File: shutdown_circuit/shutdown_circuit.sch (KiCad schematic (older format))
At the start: 16 parts

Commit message: Not sure
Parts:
- C? (x2): value C -> 1u
- C? (x2): value C -> 10u
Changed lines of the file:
@@
 LIBS:relays
 LIBS:shutdown_circuit-cache
-EELAYER 26 0
+EELAYER 25 0
 EELAYER END
 $Descr A4 11693 8268
@@
 P 1800 1100
 F 0 "C?" H 1915 1146 50  0000 L CNN
-F 1 "C" H 1915 1055 50  0000 L CNN
+F 1 "1u" H 1915 1055 50  0000 L CNN
 F 2 "" H 1838 950 50  0000 C CNN
 F 3 "" H 1800 1100 50  0000 C CNN
@@
 P 2200 1100
 F 0 "C?" H 2315 1146 50  0000 L CNN
-F 1 "C" H 2315 1055 50  0000 L CNN
+F 1 "10u" H 2315 1055 50  0000 L CNN
 F 2 "" H 2238 950 50  0000 C CNN
 F 3 "" H 2200 1100 50  0000 C CNN
@@
 P 3500 1100
 F 0 "C?" H 3615 1146 50  0000 L CNN
-F 1 "C" H 3615 1055 50  0000 L CNN
+F 1 "1u" H 3615 1055 50  0000 L CNN
 F 2 "" H 3538 950 50  0000 C CNN
 F 3 "" H 3500 1100 50  0000 C CNN
@@
 P 3950 1100
 F 0 "C?" H 4065 1146 50  0000 L CNN
-F 1 "C" H 4065 1055 50  0000 L CNN
+F 1 "10u" H 4065 1055 50  0000 L CNN
 F 2 "" H 3988 950 50  0000 C CNN
 F 3 "" H 3950 1100 50  0000 C CNN

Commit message: Shutdown circuit changes, IMD begun
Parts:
- removed P?: +12V GLV, symbol CONN_01X01
- removed P?: Ground GLV, symbol CONN_01X01
- removed P?: CONN_01X04, symbol CONN_01X04
- added P?: MX150_8, symbol MX150_8
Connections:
- wire segments 27 -> 25
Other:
- moved on the sheet: U?B
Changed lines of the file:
@@
 LIBS:contrib
 LIBS:valves
+LIBS:relays
 LIBS:UNCAMotorsports
-LIBS:relays
 LIBS:shutdown_circuit-cache
 EELAYER 25 0
@@
 	3950 950  3950 800
 Connection ~ 3950 950
-$Comp
-L +12V #PWR?
-U 1 1 58B0A6A8
-P 1800 800
-F 0 "#PWR?" H 1800 650 50  0001 C CNN
-F 1 "+12V" H 1815 973 50  0000 C CNN
-F 2 "" H 1800 800 50  0000 C CNN
-F 3 "" H 1800 800 50  0000 C CNN
-	1    1800 800
-	1    0    0    -1
-$EndComp
-Wire Wire Line
-	1800 800  1800 950
-$Comp
-L CONN_01X01 P?
-U 1 1 58B0A6D7
-P 700 950
-F 0 "P?" H 619 725 50  0000 C CNN
-F 1 "+12V GLV" H 619 816 50  0000 C CNN
-F 2 "" H 700 950 50  0000 C CNN
-F 3 "" H 700 950 50  0000 C CNN
-	1    700  950
-	-1   0    0    1
-$EndComp
 Wire Wire Line
 	900  950  1200 950
@@
 Wire Wire Line
 	1800 1350 1800 1250
-$Comp
-L CONN_01X01 P?
-U 1 1 58B0A8F1
-P 700 1450
-F 0 "P?" H 619 1225 50  0000 C CNN
-F 1 "Ground GLV" H 619 1316 50  0000 C CNN
-F 2 "" H 700 1450 50  0000 C CNN
-F 3 "" H 700 1450 50  0000 C CNN
-	1    700  1450
-	-1   0    0    1
-$EndComp
-$Comp
-L GND #PWR?
-U 1 1 58B0A96E
-P 1050 1450
-F 0 "#PWR?" H 1050 1200 50  0001 C CNN
-F 1 "GND" H 1055 1277 50  0000 C CNN
-F 2 "" H 1050 1450 50  0000 C CNN
-F 3 "" H 1050 1450 50  0000 C CNN
-	1    1050 1450
-	1    0    0    -1
-$EndComp
-Wire Wire Line
-	1050 1450 900  1450
 $Comp
 L R R?
@@
 L 74HC20D U?
 U 2 1 58B0B725
-P 3800 4600
-F 0 "U?" H 4341 4653 60  0000 L CNN
-F 1 "74HC20D" H 4341 4547 60  0000 L CNN
-F 2 "" H 3800 4600 60  0001 C CNN
-F 3 "" H 3800 4600 60  0001 C CNN
-	2    3800 4600
+P 6300 3100
+F 0 "U?" H 6841 3153 60  0000 L CNN
+F 1 "74HC20D" H 6841 3047 60  0000 L CNN
+F 2 "" H 6300 3100 60  0001 C CNN
+F 3 "" H 6300 3100 60  0001 C CNN
+	2    6300 3100
 	1    0    0    -1
 $EndComp
@@
 L +5V #PWR?
 U 1 1 58B0B835
-P 3900 4150
-F 0 "#PWR?" H 3900 4000 50  0001 C CNN
-F 1 "+5V" H 3915 4323 50  0000 C CNN
-F 2 "" H 3900 4150 50  0000 C CNN
-F 3 "" H 3900 4150 50  0000 C CNN
-	1    3900 4150
-	1    0    0    -1
-$EndComp
-Wire Wire Line
-	3900 4150 3900 4200
+P 6400 2650
+F 0 "#PWR?" H 6400 2500 50  0001 C CNN
+F 1 "+5V" H 6415 2823 50  0000 C CNN
+F 2 "" H 6400 2650 50  0000 C CNN
+F 3 "" H 6400 2650 50  0000 C CNN
+	1    6400 2650
+	1    0    0    -1
+$EndComp
+Wire Wire Line
+	6400 2650 6400 2700
 $Comp
 L GND #PWR?
 U 1 1 58B0B886
-P 3900 5050
-F 0 "#PWR?" H 3900 4800 50  0001 C CNN
-F 1 "GND" H 3905 4877 50  0000 C CNN
-F 2 "" H 3900 5050 50  0000 C CNN
-F 3 "" H 3900 5050 50  0000 C CNN
-	1    3900 5050
-	1    0    0    -1
-$EndComp
-Wire Wire Line
-	3900 5050 3900 5000
-NoConn ~ 4300 4600
-Wire Wire Line
-	3450 4200 3450 4750
-Connection ~ 3450 4550
-Connection ~ 3450 4650
-Wire Wire Line
-	3900 4200 3450 4200
-Connection ~ 3450 4450
+P 6400 3550
+F 0 "#PWR?" H 6400 3300 50  0001 C CNN
+F 1 "GND" H 6405 3377 50  0000 C CNN
+F 2 "" H 6400 3550 50  0000 C CNN
+F 3 "" H 6400 3550 50  0000 C CNN
+	1    6400 3550
+	1    0    0    -1
+$EndComp
+Wire Wire Line
+	6400 3550 6400 3500
+NoConn ~ 6800 3100
+Wire Wire Line
+	5950 2700 5950 3250
+Connection ~ 5950 3050
+Connection ~ 5950 3150
+Wire Wire Line
+	6400 2700 5950 2700
+Connection ~ 5950 2950
 $Comp
 L GND #PWR?
@@
 Connection ~ 2500 3050
 Connection ~ 2200 2950
-$Comp
-L CONN_01X04 P?
-U 1 1 58B0C0EE
-P 1750 3100
-F 0 "P?" H 1669 2725 50  0000 C CNN
-F 1 "CONN_01X04" H 1669 2816 50  0000 C CNN
-F 2 "" H 1750 3100 50  0000 C CNN
-F 3 "" H 1750 3100 50  0000 C CNN
-	1    1750 3100
-	-1   0    0    1
-$EndComp
 Wire Wire Line
 	2200 2950 2200 3250
@@
 Wire Wire Line
 	4950 2700 4950 2900
+$Comp
+L +12V #PWR?
+U 1 1 58C9C2DE
+P 900 950
+F 0 "#PWR?" H 900 800 50  0001 C CNN
+F 1 "+12V" H 900 1090 50  0000 C CNN
+F 2 "" H 900 950 50  0001 C CNN
+F 3 "" H 900 950 50  0001 C CNN
+	1    900  950
+	1    0    0    -1
+$EndComp
+$Comp
+L MX150_8 P?
+U 1 1 58C9C54A
+P 6050 1300
+F 0 "P?" H 6050 1550 50  0000 C CNN
+F 1 "MX150_8" H 6050 1050 50  0000 C CNN
+F 2 "" H 6050 100 50  0000 C CNN
+F 3 "" H 6050 100 50  0000 C CNN
+	1    6050 1300
+	1    0    0    -1
+$EndComp
 $EndSCHEMATC

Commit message: Decoupling caps annotated
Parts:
- removed P?: MX150_8, symbol MX150_8
- removed Q?: Q_PMOS_GSD, symbol Q_PMOS_GSD
- added C3: 1u, symbol C
- added D1: D, symbol D
- added R?: 1k, symbol R
- added RL1: Relay-SPST, symbol Relay-SPST
- added U?: BTS6133D, symbol BTS6133D
- gave numbers to parts that had none: 11
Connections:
- net labels added: AMS_Latched_Out, BSPD_Latched_Out, IMD_Latched_Out, Shutdown_Circuit
- wire segments 25 -> 44
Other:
- note added: "Decoupling Capacitor"
- note added: "U2A and U2B are NAND gate units on the same IC package"
- moved on the sheet: U2B

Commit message: Fixed board error on BSPD
Track near via error corrected
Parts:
- gave numbers to parts that had none: 2
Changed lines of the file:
@@
 $EndComp
 $Comp
-L GND #PWR12
+L GND #PWR15
 U 1 1 59028E75
 P 6050 4300
-F 0 "#PWR12" H 6050 4050 50  0001 C CNN
+F 0 "#PWR15" H 6050 4050 50  0001 C CNN
 F 1 "GND" H 6050 4150 50  0000 C CNN
 F 2 "" H 6050 4300 50  0001 C CNN
@@
 Connection ~ 1950 3150
 $Comp
-L BTS6133D U?
+L BTS6133D U3
 U 1 1 5902B766
 P 5200 3100
-F 0 "U?" H 5000 3350 60  0000 C CNN
+F 0 "U3" H 5000 3350 60  0000 C CNN
 F 1 "BTS6133D" H 5250 2850 60  0000 C CNN
 F 2 "" H 5350 3300 60  0000 C CNN
@@
 	4350 3100 4800 3100
 $Comp
-L R R?
+L R R5
 U 1 1 5902C3F4
 P 4800 3550
-F 0 "R?" V 4880 3550 50  0000 C CNN
+F 0 "R5" V 4880 3550 50  0000 C CNN
 F 1 "1k" V 4800 3550 50  0000 C CNN
 F 2 "" V 4730 3550 50  0001 C CNN
@@
 	4800 3200 4800 3400
 $Comp
-L GND #PWR?
+L GND #PWR12
 U 1 1 5902C486
 P 4800 3700
-F 0 "#PWR?" H 4800 3450 50  0001 C CNN
+F 0 "#PWR12" H 4800 3450 50  0001 C CNN
 F 1 "GND" H 4800 3550 50  0000 C CNN
 F 2 "" H 4800 3700 50  0001 C CNN
@@
 $EndComp
 $Comp
-L +12V #PWR?
+L +12V #PWR11
 U 1 1 5902C52C
 P 4800 2850
-F 0 "#PWR?" H 4800 2700 50  0001 C CNN
+F 0 "#PWR11" H 4800 2700 50  0001 C CNN
 F 1 "+12V" H 4800 2990 50  0000 C CNN
 F 2 "" H 4800 2850 50  0001 C CNN

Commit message: ??
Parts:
- removed C1: 1u, symbol C
- removed C5: 10u, symbol C
- added J1: Shutdown_Circuit, symbol CONN_01X02
- C1: renamed from C2; value 10u -> 1u
- renumbered C3 to C2, C4 to C3
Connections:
- net Shutdown_Circuit: now also J1.1 (P1), J1.2 (P2)
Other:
- moved on the sheet: C1
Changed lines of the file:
@@
 $Comp
 L C C1
-U 1 1 58B0A511
-P 1800 1100
-F 0 "C1" H 1915 1146 50  0000 L CNN
-F 1 "1u" H 1915 1055 50  0000 L CNN
-F 2 "" H 1838 950 50  0000 C CNN
-F 3 "" H 1800 1100 50  0000 C CNN
-	1    1800 1100
-	1    0    0    -1
-$EndComp
-$Comp
-L C C2
 U 1 1 58B0A559
-P 2200 1100
-F 0 "C2" H 2315 1146 50  0000 L CNN
-F 1 "10u" H 2315 1055 50  0000 L CNN
-F 2 "" H 2238 950 50  0000 C CNN
-F 3 "" H 2200 1100 50  0000 C CNN
-	1    2200 1100
+P 2250 1100
+F 0 "C1" H 2365 1146 50  0000 L CNN
+F 1 "1u" H 2365 1055 50  0000 L CNN
+F 2 "" H 2288 950 50  0000 C CNN
+F 3 "" H 2250 1100 50  0000 C CNN
+	1    2250 1100
 	1    0    0    -1
 $EndComp
@@
 $EndComp
 $Comp
-L C C4
+L C C3
 U 1 1 58B0A5AD
 P 3500 1100
-F 0 "C4" H 3615 1146 50  0000 L CNN
+F 0 "C3" H 3615 1146 50  0000 L CNN
 F 1 "1u" H 3615 1055 50  0000 L CNN
 F 2 "" H 3538 950 50  0000 C CNN
@@
 	1    0    0    -1
 $EndComp
-$Comp
-L C C5
-U 1 1 58B0A5FF
-P 3950 1100
-F 0 "C5" H 4065 1146 50  0000 L CNN
-F 1 "10u" H 4065 1055 50  0000 L CNN
-F 2 "" H 3988 950 50  0000 C CNN
-F 3 "" H 3950 1100 50  0000 C CNN
-	1    3950 1100
-	1    0    0    -1
-$EndComp
 Wire Wire Line
 	1500 950  2550 950
-Connection ~ 1800 950
-Connection ~ 2200 950
-Wire Wire Line
-	3150 950  3950 950
-Connection ~ 3500 950
 $Comp
 L +5V #PWR8
 U 1 1 58B0A679
-P 3950 800
-F 0 "#PWR8" H 3950 650 50  0001 C CNN
-F 1 "+5V" H 3965 973 50  0000 C CNN
-F 2 "" H 3950 800 50  0000 C CNN
-F 3 "" H 3950 800 50  0000 C CNN
-	1    3950 800
-	1    0    0    -1
-$EndComp
-Wire Wire Line
-	3950 950  3950 800
-Connection ~ 3950 950
+P 3500 900
+F 0 "#PWR8" H 3500 750 50  0001 C CNN
+F 1 "+5V" H 3515 1073 50  0000 C CNN
+F 2 "" H 3500 900 50  0000 C CNN
+F 3 "" H 3500 900 50  0000 C CNN
+	1    3500 900
+	1    0    0    -1
+$EndComp
 Wire Wire Line
 	900  950  1200 950
-Wire Wire Line
-	1800 1250 3950 1250
-Connection ~ 2200 1250
-Connection ~ 2850 1250
-Connection ~ 3500 1250
-$Comp
-L GND #PWR2
+$Comp
+L GND #PWR5
 U 1 1 58B0A873
-P 1800 1350
-F 0 "#PWR2" H 1800 1100 50  0001 C CNN
-F 1 "GND" H 1805 1177 50  0000 C CNN
-F 2 "" H 1800 1350 50  0000 C CNN
-F 3 "" H 1800 1350 50  0000 C CNN
-	1    1800 1350
-	1    0    0    -1
-$EndComp
-Wire Wire Line
-	1800 1350 1800 1250
+P 2850 1350
+F 0 "#PWR5" H 2850 1100 50  0001 C CNN
+F 1 "GND" H 2855 1177 50  0000 C CNN
+F 2 "" H 2850 1350 50  0000 C CNN
+F 3 "" H 2850 1350 50  0000 C CNN
+	1    2850 1350
+	1    0    0    -1
+$EndComp
 $Comp
 L R R1
@@
 $EndComp
 $Comp
-L GND #PWR5
+L GND #PWR4
 U 1 1 58B0BA55
 P 2800 3600
-F 0 "#PWR5" H 2800 3350 50  0001 C CNN
+F 0 "#PWR4" H 2800 3350 50  0001 C CNN
 F 1 "GND" H 2805 3427 50  0000 C CNN
 F 2 "" H 2800 3600 50  0000 C CNN
@@
 $EndComp
 $Comp
-L GND #PWR4
+L GND #PWR3
 U 1 1 58B0BA85
 P 2500 3600
-F 0 "#PWR4" H 2500 3350 50  0001 C CNN
+F 0 "#PWR3" H 2500 3350 50  0001 C CNN
 F 1 "GND" H 2505 3427 50  0000 C CNN
 F 2 "" H 2500 3600 50  0000 C CNN
@@
 $EndComp
 $Comp
-L GND #PWR3
+L GND #PWR2
 U 1 1 58B0BAB5
 P 2200 3600
-F 0 "#PWR3" H 2200 3350 50  0001 C CNN
+F 0 "#PWR2" H 2200 3350 50  0001 C CNN
 F 1 "GND" H 2205 3427 50  0000 C CNN
 F 2 "" H 2200 3600 50  0000 C CNN
@@
 	6050 4300 6050 4250
 $Comp
-L C C3
+L C C2
 U 1 1 590294EC
 P 3450 2650
-F 0 "C3" H 3475 2750 50  0000 L CNN
+F 0 "C2" H 3475 2750 50  0000 L CNN
 F 1 "1u" H 3475 2550 50  0000 L CNN
 F 2 "" H 3488 2500 50  0001 C CNN
@@
 Wire Wire Line
 	4800 2850 4800 3000
+Wire Wire Line
+	3150 950  3500 950
+Wire Wire Line
+	3500 950  3500 900
+Wire Wire Line
+	2250 1250 3500 1250
+Connection ~ 2250 950
+Connection ~ 2850 1250
+Wire Wire Line
+	2850 1250 2850 1350
+$Comp
+L CONN_01X02 J1
+U 1 1 5913E7C7
+P 7850 3950
+F 0 "J1" H 7850 4100 50  0000 C CNN
+F 1 "Shutdown_Circuit" V 7950 3950 50  0000 C CNN
+F 2 "" H 7850 3950 50  0001 C CNN
+F 3 "" H 7850 3950 50  0001 C CNN
+	1    7850 3950
+	1    0    0    -1
+$EndComp
+Wire Wire Line
+	7650 3650 7650 3900
+Wire Wire Line
+	7650 4000 7650 4250
 $EndSCHEMATC

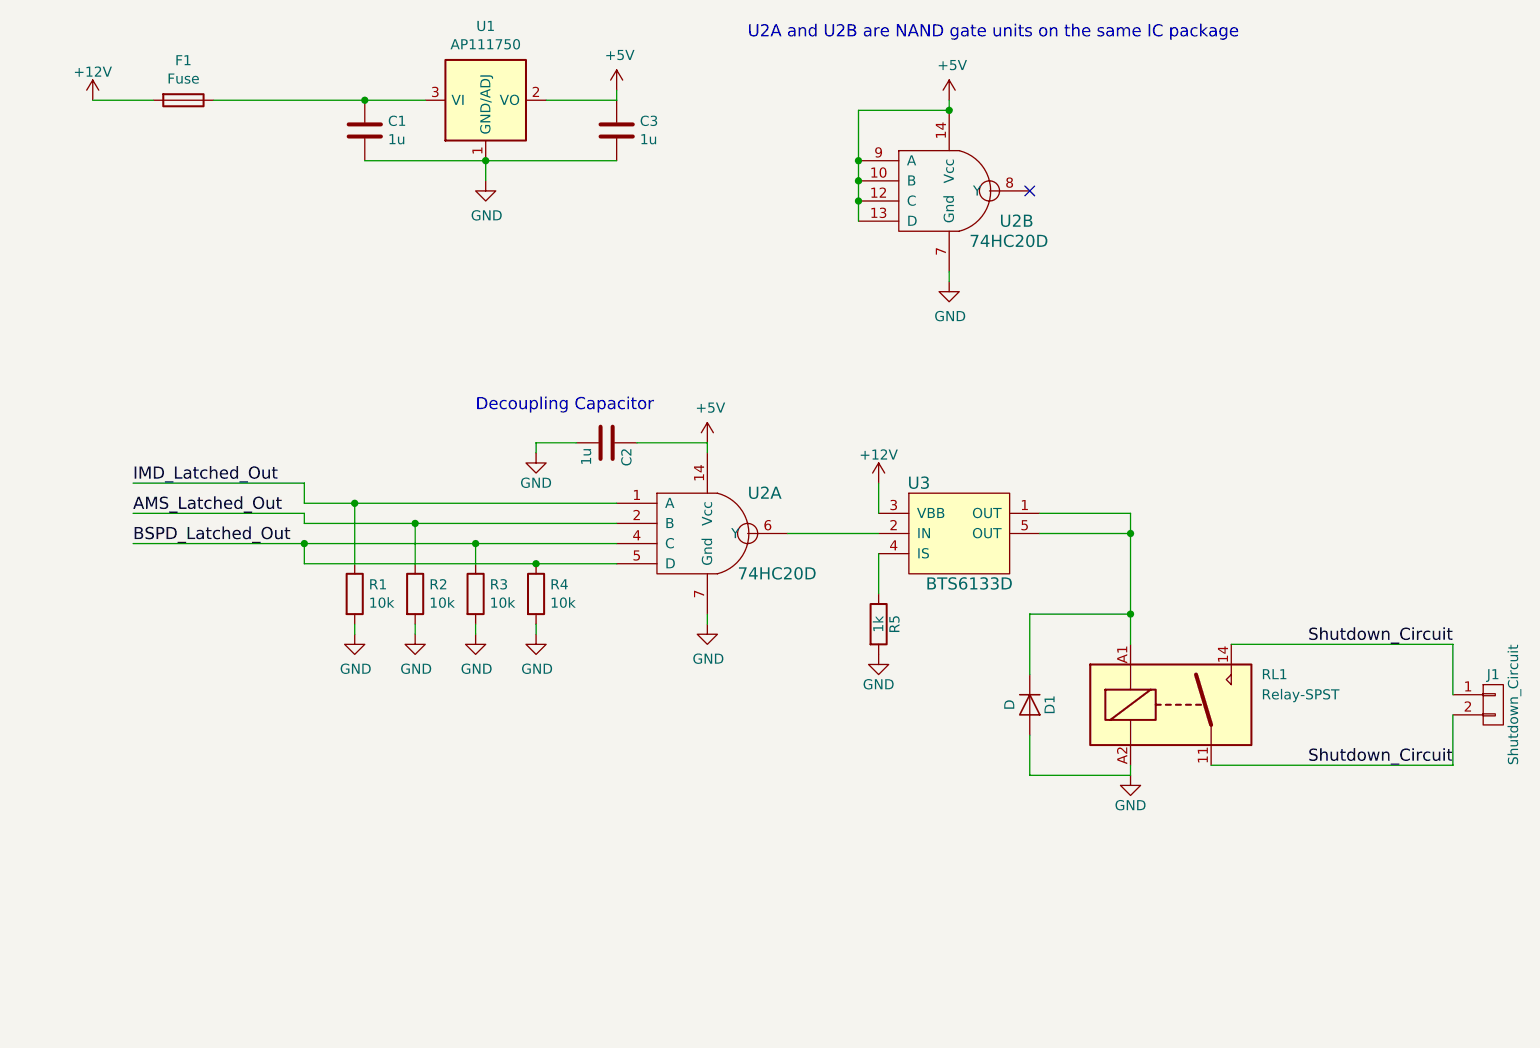
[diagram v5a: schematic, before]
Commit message: SCRB layout done
Shutdown Circuit Relay Board
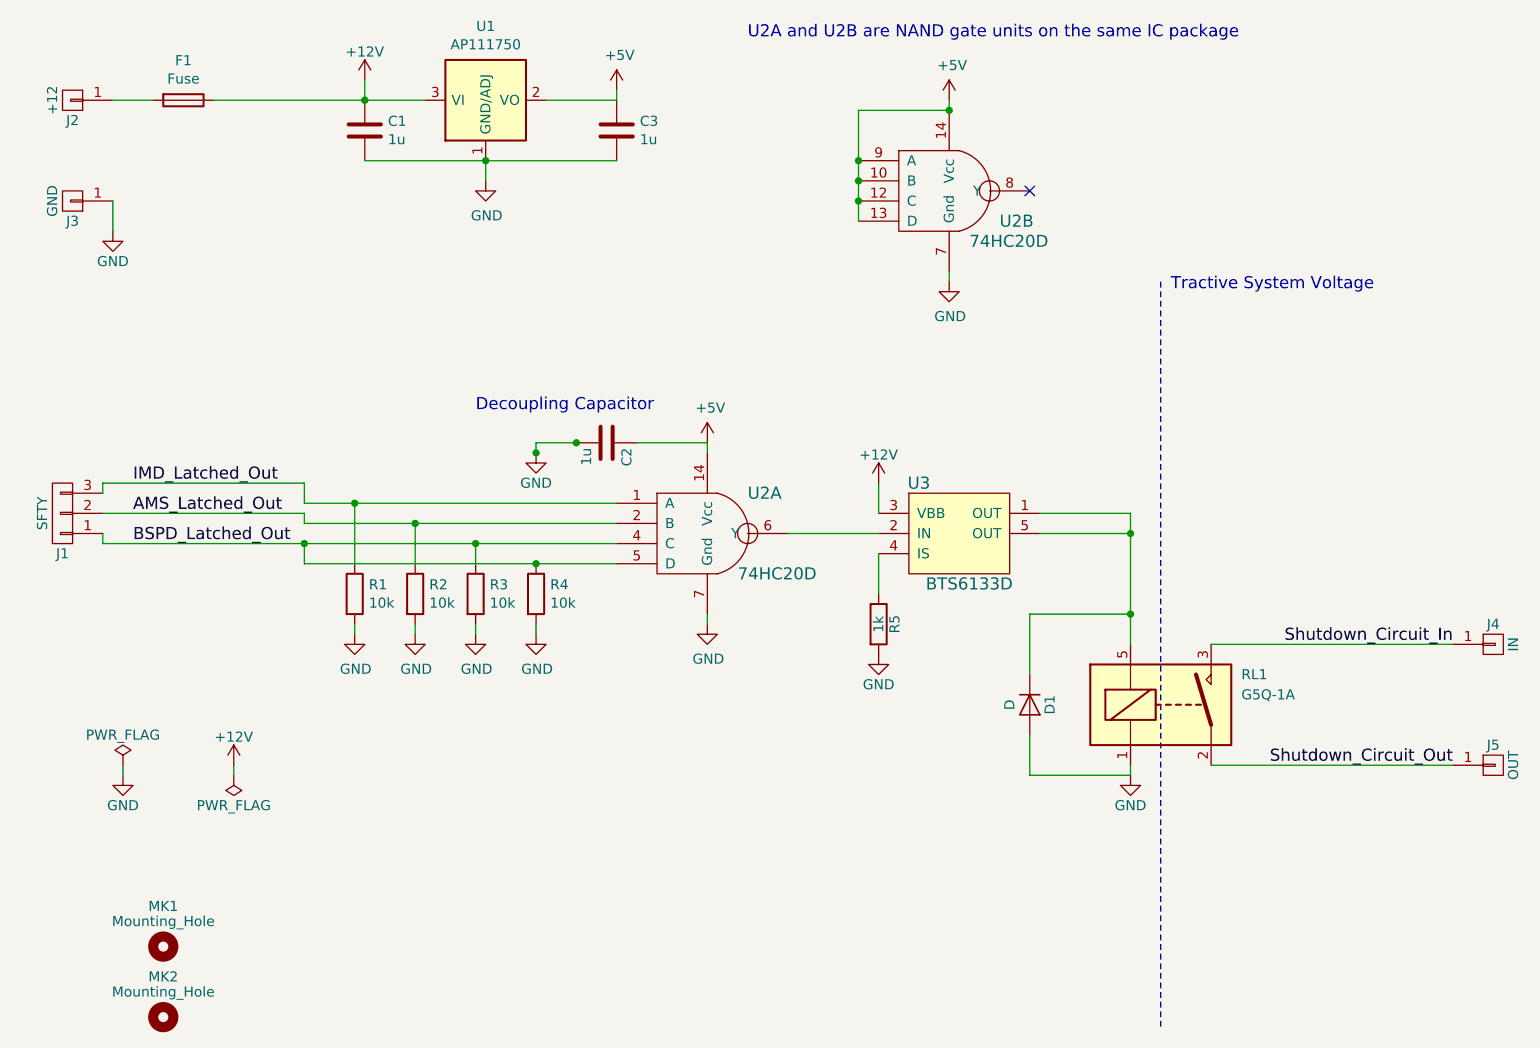
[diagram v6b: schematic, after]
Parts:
- removed J1: Shutdown_Circuit, symbol CONN_01X02
- removed RL1: Relay-SPST, symbol Relay-SPST
- added J1: SFTY, Pin_Headers:Pin_Header_Straight_1x03_Pitch2.54mm, symbol CONN_01X03
- added J2: +12, Wire_Pads:SolderWirePad_single_1-2mmDrill, symbol CONN_01X01
- added J3: GND, Wire_Pads:SolderWirePad_single_1-2mmDrill, symbol CONN_01X01
- added J4: IN, Wire_Pads:SolderWirePad_single_1-2mmDrill, symbol CONN_01X01
- added J5: OUT, Wire_Pads:SolderWirePad_single_1-2mmDrill, symbol CONN_01X01
- added MK1, MK2: Mounting_Hole, Mounting_Holes:MountingHole_3mm, symbol Mounting_Hole
- added RL1: G5Q-1A, Relays_THT:Relay_SPST-NO_OMRON-G5Q, symbol G5Q-1A
- C1, C2, C3: footprint (none) -> Capacitors_SMD:C_0805_HandSoldering
- D1: footprint (none) -> Diodes_ThroughHole:D_DO-41_SOD81_P7.62mm_Horizontal
- F1: footprint (none) -> SMD_Packages:SMD-1210_Pol
- R1, R2, R3, R4, R5: footprint (none) -> Resistors_SMD:R_0805_HandSoldering
- U2: footprint (none) -> Housings_SOIC:SOIC-14_3.9x8.7mm_Pitch1.27mm
- U3: footprint (none) -> UNCAMotorsports:TO-252-5
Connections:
- net +12V: now also C1.1, F1.1, U1.3 (VI); no longer F1.2
- net AMS_Latched_Out: now also J1.2 (P2)
- net BSPD_Latched_Out: now also J1.1 (P1)
- net GND: now also J3.1 (P1), RL1.1
- net IMD_Latched_Out: now also J1.3 (P3)
- net at D1.1 (K), U3.1 (OUT), U3.5 (OUT): now also RL1.5
- new net: F1.2, J2.1 (P1)
- new net Shutdown_Circuit_In: J4.1 (P1), RL1.3
- new net Shutdown_Circuit_Out: J5.1 (P1), RL1.2
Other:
- note added: "Tractive System Voltage\n"
